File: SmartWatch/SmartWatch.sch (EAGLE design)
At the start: 5 parts, among them Q1 32.768 kHz (501HCAM032768CAF), Q2 16 MHz (501BAA16M0000CAF)

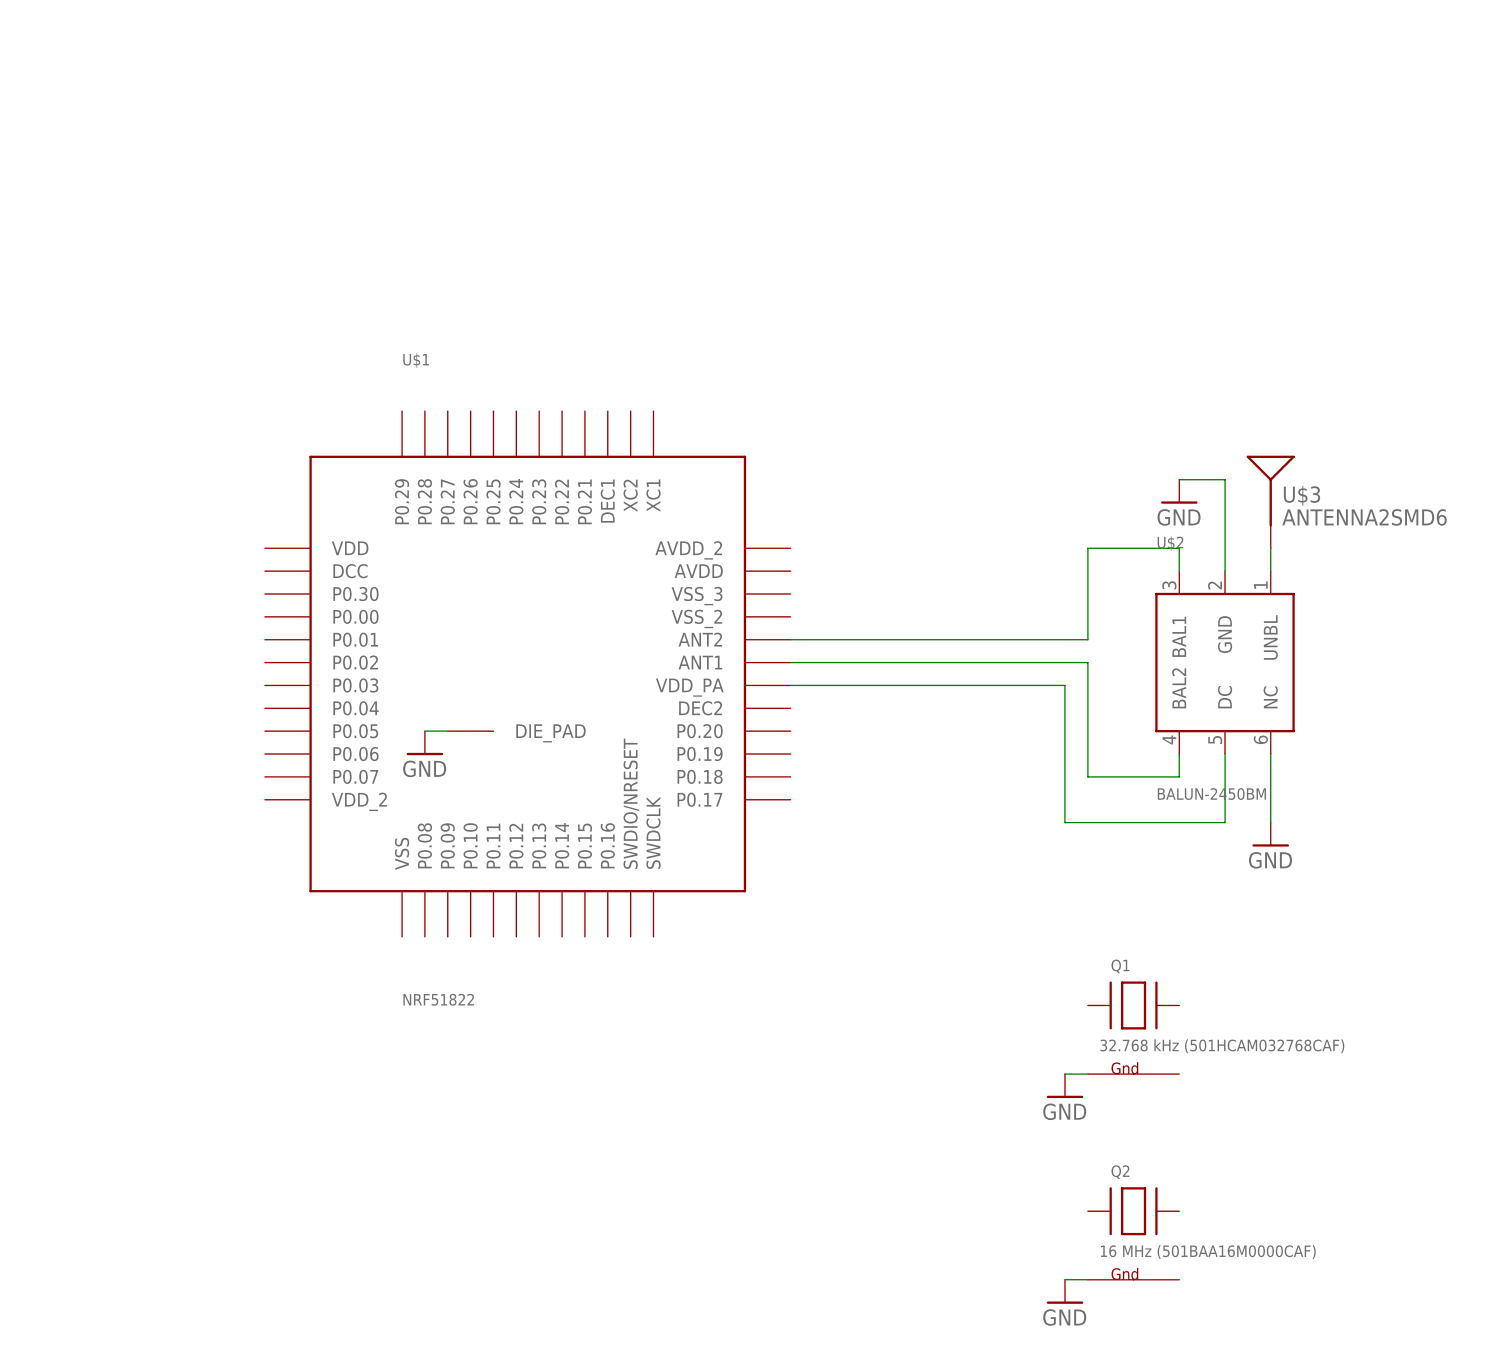
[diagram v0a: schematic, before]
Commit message: Schematic update.
Added and connected antenna and top,right,bottom of Nordic IC
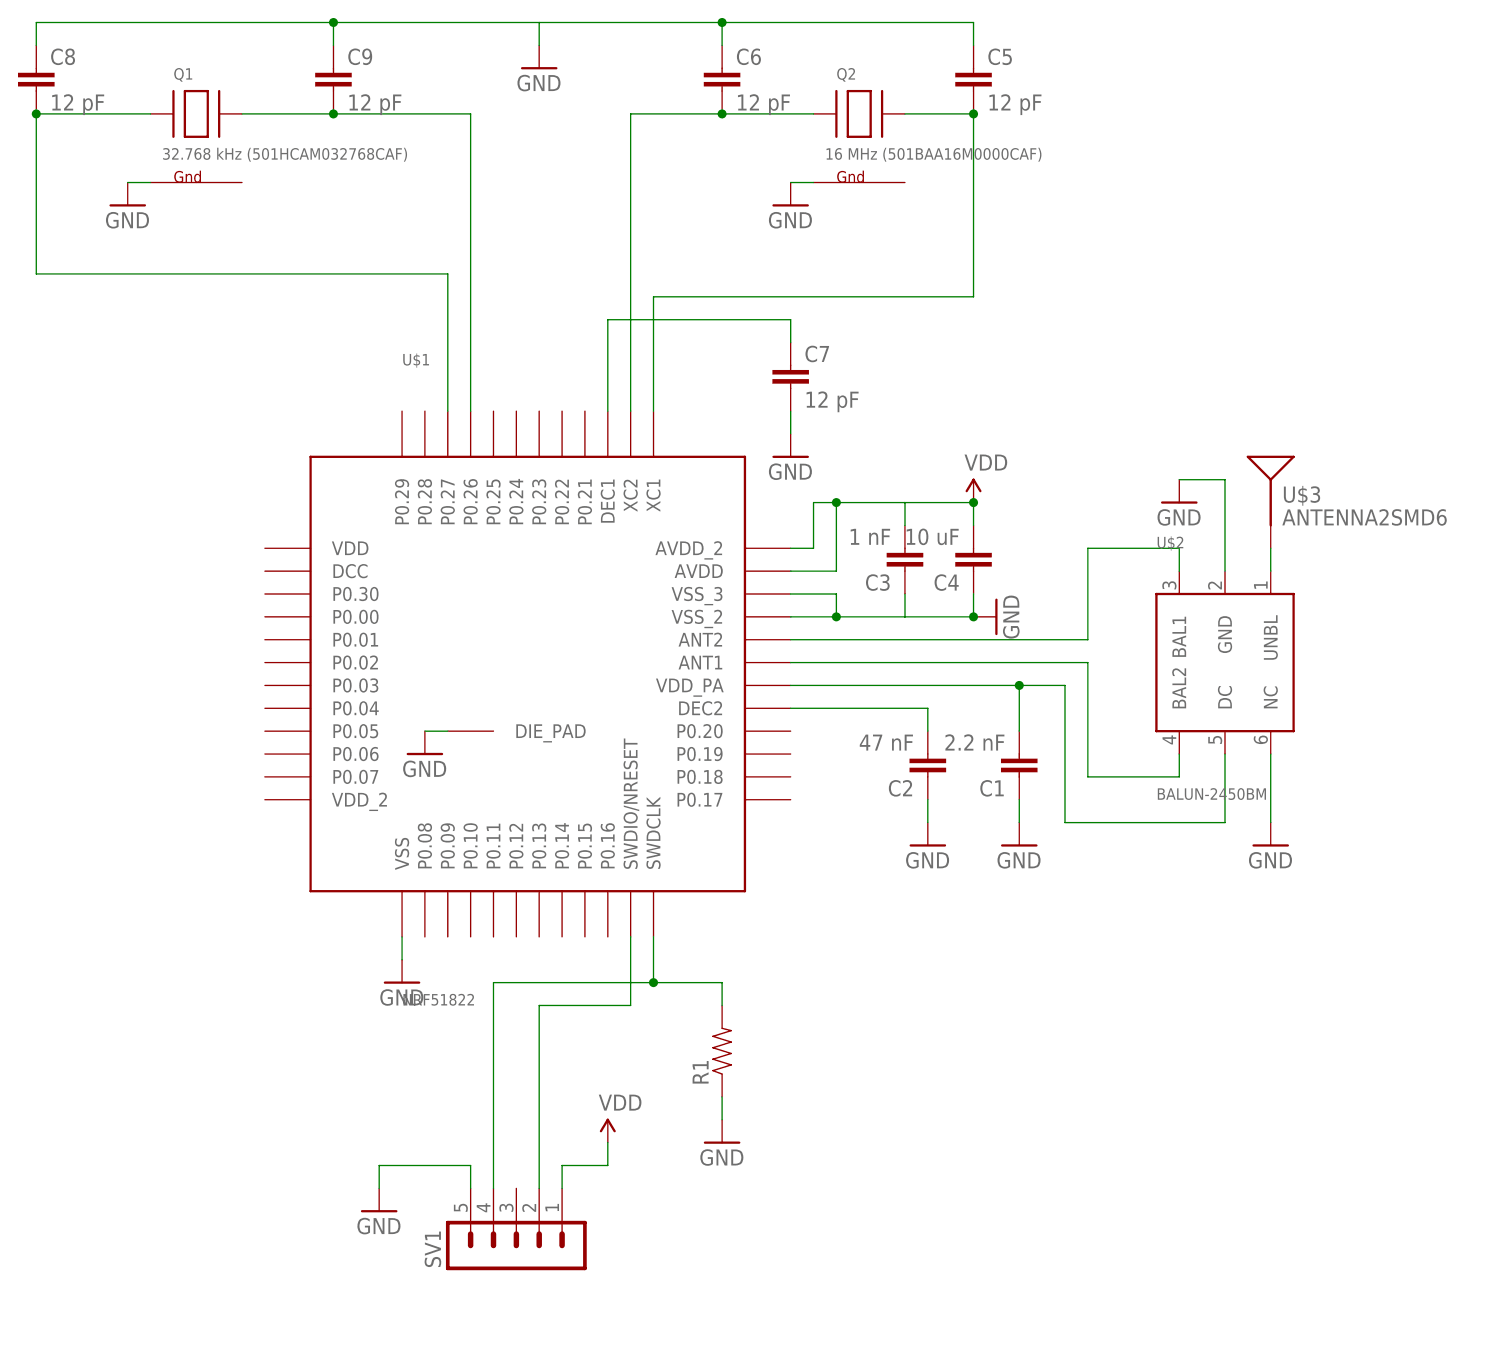
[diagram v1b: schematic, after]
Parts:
- added C1: 2.2 nF, SparkFun-Capacitors:CAP0603-CAP
- added C2: 47 nF, SparkFun-Capacitors:CAP0603-CAP
- added C3: 1 nF, SparkFun-Capacitors:CAP0603-CAP
- added C4: 10 uF, SparkFun-Capacitors:CAP0603-CAP
- added C5, C6, C7, C8, C9: 12 pF, SparkFun-Capacitors:CAP0603-CAP
- added R1: (no value), SparkFun-Resistors:RESISTOR0603-RES
- added SV1: (no value), con-lstb:MA05-1
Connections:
- new net N$10: C7.1, U$1.DEC1
- new net N$12: C9.2, Q1.X2, U$1.P0.26
- new net N$13: C8.2, Q1.X1, U$1.P0.27
- new net N$16: SV1.2, U$1.SWDIO/NRESET
- new net N$3: C6.2, Q2.X1, U$1.XC2
- new net N$4: C2.2, U$1.DEC2
- new net N$6: C5.2, Q2.X2, U$1.XC1
- new net N$9: R1.2, SV1.4, U$1.SWDCLK
- new net VDD: C3.2, C4.2, SV1.1, U$1.AVDD, U$1.AVDD_2
- net GND: now also C1.1, C2.1, C3.1, C4.1, C5.1, C6.1, C7.2, C8.1, C9.1, R1.1, SV1.5, U$1.VSS, U$1.VSS_2, U$1.VSS_3
- net N$5: now also C1.2
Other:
- moved on the sheet: Q1, Q2
